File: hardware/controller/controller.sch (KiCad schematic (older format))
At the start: 54 parts, among them J1 USB_B_Micro, J2 Conn_01x12_Female, J3 Cooling fan, U1 DS3231MZ, U2 LMR16006YQ5, U3 ESP32-WROOM, U4 LMR16006YQ5, U5 CP2102N-A01-GQFN24

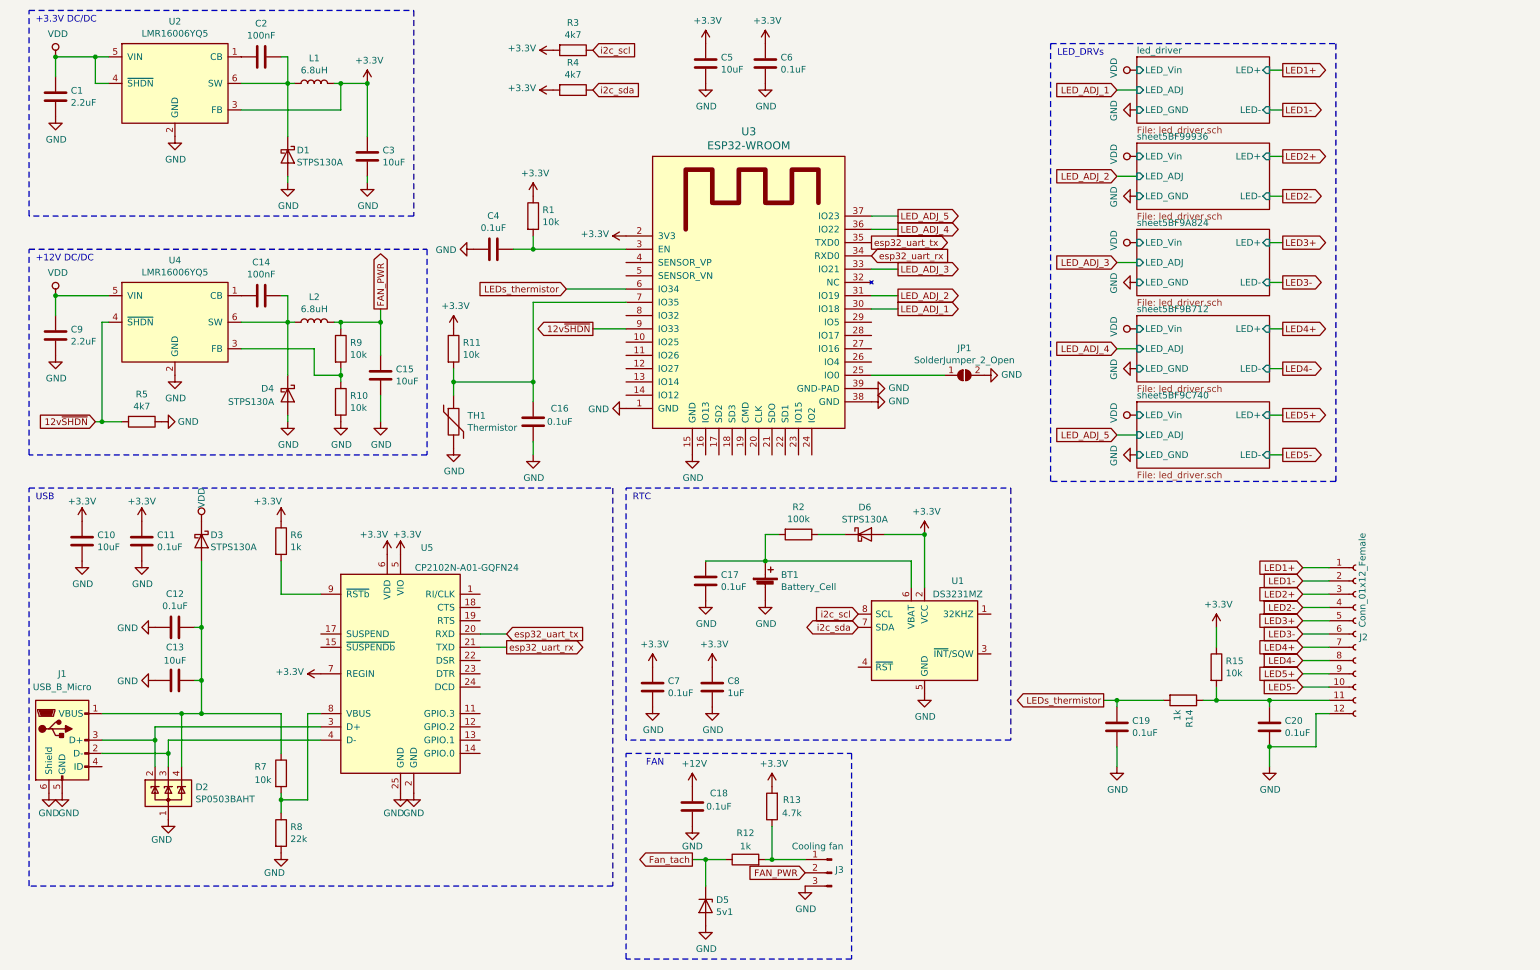
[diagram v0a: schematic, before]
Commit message: initial controller components placement
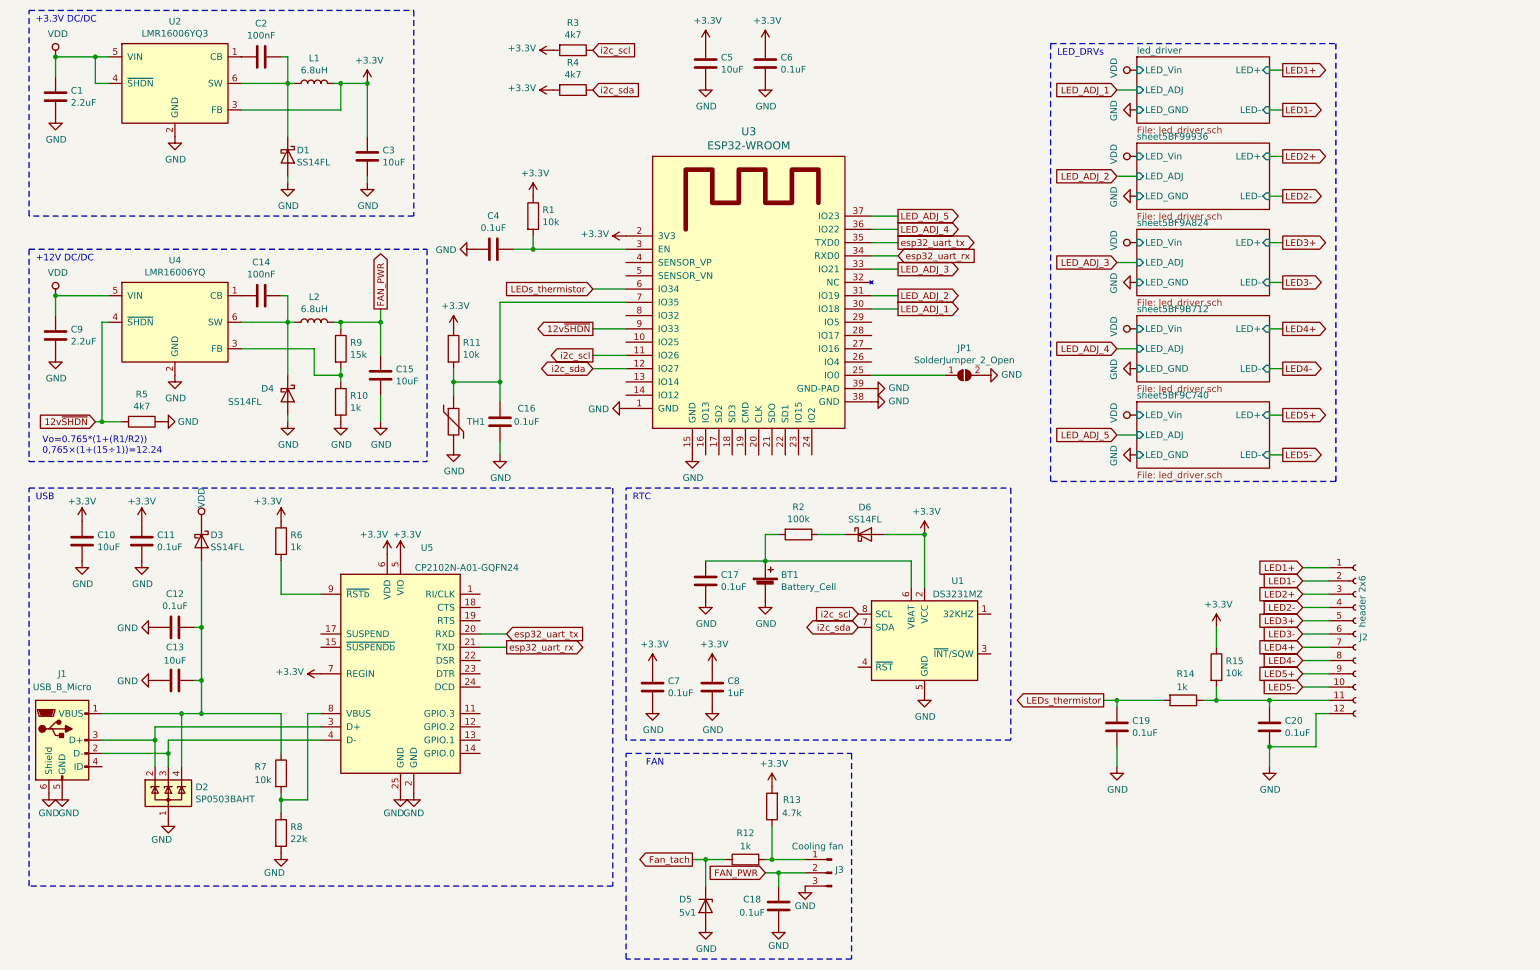
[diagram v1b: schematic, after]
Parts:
- D1, D3, D4, D6: value STPS130A -> SS14FL; footprint Diode_SMD:D_SMA -> Diode_SMD:D_SOD-123F
- J1: footprint Connector_USB:USB_Micro-B_Molex-105133-0001 -> led:USB_Micro-B_Molex-105017-0001
- J2: value Conn_01x12_Female -> header 2x6
- L1, L2: footprint Inductor_SMD:L_Wuerth_MAPI-4030 -> Inductor_SMD:L_Wuerth_MAPI-3015
- R10: value 10k -> 1k
- R9: value 10k -> 15k
- TH1: value Thermistor -> NTCS0603E3103
- U2: value LMR16006YQ5 -> LMR16006YQ3
- U4: value LMR16006YQ5 -> LMR16006YQ
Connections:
- net +12V is gone; now on net FAN_PWR: C18.2
- net i2c_scl: now also U3.11 (IO26)
- net i2c_sda: now also U3.12 (IO27)
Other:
- note added: "Vo=0.765*(1+(R1/R2))\n0,765×(1+(15÷1))=12.24"
- moved on the sheet: C16, C18
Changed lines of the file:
@@
 P 1700 1150
 F 0 "U2" H 1700 1617 50  0000 C CNN
-F 1 "LMR16006YQ5" H 1700 1526 50  0000 C CNN
+F 1 "LMR16006YQ3" H 1700 1526 50  0000 C CNN
 F 2 "Package_TO_SOT_SMD:SOT-23-6" H 1700 650 50  0001 C CIN
 F 3 "http://www.ti.com/lit/ds/symlink/lmr16006y-q1.pdf" H 1300 1600 50  0001 C CNN
@@
 F 0 "L1" V 2940 1150 50  0000 C CNN
 F 1 "6.8uH" V 2849 1150 50  0000 C CNN
-F 2 "Inductor_SMD:L_Wuerth_MAPI-4030" H 2750 1150 50  0001 C CNN
-F 3 "~" H 2750 1150 50  0001 C CNN
+F 2 "Inductor_SMD:L_Wuerth_MAPI-3015" H 2750 1150 50  0001 C CNN
+F 3 "https://katalog.we-online.de/pbs/datasheet/74438335068.pdf" H 2750 1150 50  0001 C CNN
 	1    2750 1150
 	0    -1   -1   0
@@
 P 2550 1700
 F 0 "D1" V 2504 1768 50  0000 L CNN
-F 1 "STPS130A" V 2595 1768 50  0000 L CNN
-F 2 "Diode_SMD:D_SMA" H 2550 1700 50  0001 C CNN
+F 1 "SS14FL" V 2595 1768 50  0000 L CNN
+F 2 "Diode_SMD:D_SOD-123F" H 2550 1700 50  0001 C CNN
 F 3 "~" H 2550 1700 50  0001 C CNN
 	1    2550 1700
@@
 F 0 "J1" H 850 6600 50  0000 C CNN
 F 1 "USB_B_Micro" H 850 6500 50  0000 C CNN
-F 2 "Connector_USB:USB_Micro-B_Molex-105133-0001" H 1000 6050 50  0001 C CNN
+F 2 "led:USB_Micro-B_Molex-105017-0001" H 1000 6050 50  0001 C CNN
 F 3 "~" H 1000 6050 50  0001 C CNN
 	1    850  6100
@@
 P 6900 4550
 F 0 "D6" H 6900 4755 50  0000 C CNN
-F 1 "STPS130A" H 6900 4664 50  0000 C CNN
-F 2 "Diode_SMD:D_SMA" H 6900 4550 50  0001 C CNN
+F 1 "SS14FL" H 6900 4664 50  0000 C CNN
+F 2 "Diode_SMD:D_SOD-123F" H 6900 4550 50  0001 C CNN
 F 3 "~" H 6900 4550 50  0001 C CNN
 	1    6900 4550
@@
 P 1900 4600
 F 0 "D3" V 1854 4668 50  0000 L CNN
-F 1 "STPS130A" V 1945 4668 50  0000 L CNN
-F 2 "Diode_SMD:D_SMA" H 1900 4600 50  0001 C CNN
+F 1 "SS14FL" V 1945 4668 50  0000 L CNN
+F 2 "Diode_SMD:D_SOD-123F" H 1900 4600 50  0001 C CNN
 F 3 "~" H 1900 4600 50  0001 C CNN
 	1    1900 4600
@@
 	1    0    0    -1
 $EndComp
-Text GLabel 6950 2450 2    50   Input ~ 0
+Text GLabel 7150 2450 2    50   Input ~ 0
 esp32_uart_rx
-Text GLabel 6950 2350 2    50   Output ~ 0
+Text GLabel 7150 2350 2    50   Output ~ 0
 esp32_uart_tx
 Text GLabel 4200 5400 2    50   Output ~ 0
@@
 P 10600 5300
 F 0 "J2" H 10627 5276 50  0000 L CNN
-F 1 "Conn_01x12_Female" V 10650 5350 50  0000 L CNN
+F 1 "header 2x6" V 10650 5350 50  0000 L CNN
 F 2 "Connector_PinHeader_2.54mm:PinHeader_2x06_P2.54mm_Vertical" H 10600 5300 50  0001 C CNN
 F 3 "~" H 10600 5300 50  0001 C CNN
@@
 LEDs_thermistor
 Connection ~ 9950 5800
-Text GLabel 4650 2700 0    50   Input ~ 0
+Text GLabel 4850 2700 0    50   Input ~ 0
 LEDs_thermistor
-Wire Wire Line
-	5100 2700 4650 2700
 $Comp
 L Device:R R14
 U 1 1 5BFD7FBB
 P 9300 5800
-F 0 "R14" H 9370 5846 50  0000 L CNN
-F 1 "1k" H 9370 5755 50  0000 L CNN
+F 0 "R14" V 9100 5750 50  0000 L CNN
+F 1 "1k" V 9200 5750 50  0000 L CNN
 F 2 "Resistor_SMD:R_0603_1608Metric_Pad1.05x0.95mm_HandSolder" V 9230 5800 50  0001 C CNN
 F 3 "~" H 9300 5800 50  0001 C CNN
@@
 U 1 1 5BFF6AF0
 P 3800 3700
-F 0 "TH1" H 3905 3746 50  0000 L CNN
-F 1 "Thermistor" H 3905 3655 50  0000 L CNN
+F 0 "TH1" H 3900 3700 50  0000 L CNN
+F 1 "NTCS0603E3103" H 3905 3655 50  0001 L CNN
 F 2 "Resistor_SMD:R_0603_1608Metric_Pad1.05x0.95mm_HandSolder" H 3800 3700 50  0001 C CNN
 F 3 "~" H 3800 3700 50  0001 C CNN
@@
 L Device:C C16
 U 1 1 5BFFBB68
-P 4400 3700
-F 0 "C16" H 4200 3600 50  0000 C CNN
-F 1 "0.1uF" H 4200 3700 50  0000 C CNN
-F 2 "Capacitor_SMD:C_0603_1608Metric_Pad1.05x0.95mm_HandSolder" H 4438 3550 50  0001 C CNN
-F 3 "~" H 4400 3700 50  0001 C CNN
-	1    4400 3700
+P 4150 3700
+F 0 "C16" H 3950 3600 50  0000 C CNN
+F 1 "0.1uF" H 3950 3700 50  0000 C CNN
+F 2 "Capacitor_SMD:C_0603_1608Metric_Pad1.05x0.95mm_HandSolder" H 4188 3550 50  0001 C CNN
+F 3 "~" H 4150 3700 50  0001 C CNN
+	1    4150 3700
 	-1   0    0    1
 $EndComp
@@
 L power:GND #PWR0161
 U 1 1 5BFFBC32
-P 4400 3950
-F 0 "#PWR0161" H 4400 3700 50  0001 C CNN
-F 1 "GND" H 4405 3777 50  0000 C CNN
-F 2 "" H 4400 3950 50  0001 C CNN
-F 3 "" H 4400 3950 50  0001 C CNN
-	1    4400 3950
-	1    0    0    -1
-$EndComp
-Wire Wire Line
-	5100 2800 4400 2800
-Wire Wire Line
-	4400 2800 4400 3400
+P 4150 3950
+F 0 "#PWR0161" H 4150 3700 50  0001 C CNN
+F 1 "GND" H 4155 3777 50  0000 C CNN
+F 2 "" H 4150 3950 50  0001 C CNN
+F 3 "" H 4150 3950 50  0001 C CNN
+	1    4150 3950
+	1    0    0    -1
+$EndComp
+Wire Wire Line
+	4150 2800 4150 3400
 Wire Wire Line
 	3800 3400 3800 3300
-Connection ~ 4400 3400
-Wire Wire Line
-	4400 3400 4400 3550
+Connection ~ 4150 3400
+Wire Wire Line
+	4150 3400 4150 3550
 Wire Wire Line
 	3800 3500 3800 3400
 Connection ~ 3800 3400
 Wire Wire Line
-	4400 3950 4400 3850
+	4150 3950 4150 3850
 $Comp
 L Regulator_Switching:LMR16006YQ5 U4
@@
 P 1700 2950
 F 0 "U4" H 1700 3417 50  0000 C CNN
-F 1 "LMR16006YQ5" H 1700 3326 50  0000 C CNN
+F 1 "LMR16006YQ" H 1700 3326 50  0000 C CNN
 F 2 "Package_TO_SOT_SMD:SOT-23-6" H 1700 2450 50  0001 C CIN
 F 3 "http://www.ti.com/lit/ds/symlink/lmr16006y-q1.pdf" H 1300 3400 50  0001 C CNN
@@
 F 0 "L2" V 2940 2950 50  0000 C CNN
 F 1 "6.8uH" V 2849 2950 50  0000 C CNN
-F 2 "Inductor_SMD:L_Wuerth_MAPI-4030" H 2750 2950 50  0001 C CNN
-F 3 "~" H 2750 2950 50  0001 C CNN
+F 2 "Inductor_SMD:L_Wuerth_MAPI-3015" H 2750 2950 50  0001 C CNN
+F 3 "https://katalog.we-online.de/pbs/datasheet/74438335068.pdf" H 2750 2950 50  0001 C CNN
 	1    2750 2950
 	0    -1   -1   0
@@
 P 2550 3500
 F 0 "D4" V 2500 3300 50  0000 L CNN
-F 1 "STPS130A" V 2600 3050 50  0000 L CNN
-F 2 "Diode_SMD:D_SMA" H 2550 3500 50  0001 C CNN
+F 1 "SS14FL" V 2600 3050 50  0000 L CNN
+F 2 "Diode_SMD:D_SOD-123F" H 2550 3500 50  0001 C CNN
 F 3 "~" H 2550 3500 50  0001 C CNN
 	1    2550 3500
@@
 P 2950 3150
 F 0 "R9" H 3020 3196 50  0000 L CNN
-F 1 "10k" H 3020 3105 50  0000 L CNN
+F 1 "15k" H 3020 3105 50  0000 L CNN
 F 2 "Resistor_SMD:R_0603_1608Metric_Pad1.05x0.95mm_HandSolder" V 2880 3150 50  0001 C CNN
 F 3 "~" H 2950 3150 50  0001 C CNN
@@
 $EndComp
 Wire Wire Line
-	4400 3400 3800 3400
+	4150 3400 3800 3400
 $Comp
 L Device:R R10
@@
 P 2950 3550
 F 0 "R10" H 3020 3596 50  0000 L CNN
-F 1 "10k" H 3020 3505 50  0000 L CNN
+F 1 "1k" H 3020 3505 50  0000 L CNN
 F 2 "Resistor_SMD:R_0603_1608Metric_Pad1.05x0.95mm_HandSolder" V 2880 3550 50  0001 C CNN
 F 3 "~" H 2950 3550 50  0001 C CNN
@@
 Wire Wire Line
 	3250 2950 3250 3200
-Wire Notes Line
-	600  2400 3600 2400
-Wire Notes Line
-	3600 2400 3600 3950
-Wire Notes Line
-	3600 3950 600  3950
-Wire Notes Line
-	600  3950 600  2400
 Text GLabel 1100 3700 0    50   Input ~ 0
 12v~SHDN
@@
 L Device:C C18
 U 1 1 5C071B0A
-P 5600 6600
-F 0 "C18" H 5400 6500 50  0000 C CNN
-F 1 "0.1uF" H 5400 6600 50  0000 C CNN
-F 2 "Capacitor_SMD:C_0603_1608Metric_Pad1.05x0.95mm_HandSolder" H 5638 6450 50  0001 C CNN
-F 3 "~" H 5600 6600 50  0001 C CNN
-	1    5600 6600
+P 6250 7350
+F 0 "C18" H 6450 7300 50  0000 C CNN
+F 1 "0.1uF" H 6450 7400 50  0000 C CNN
+F 2 "Capacitor_SMD:C_0603_1608Metric_Pad1.05x0.95mm_HandSolder" H 6288 7200 50  0001 C CNN
+F 3 "~" H 6250 7350 50  0001 C CNN
+	1    6250 7350
 	-1   0    0    1
 $EndComp
@@
 P 6450 7200
 F 0 "#PWR0171" H 6450 6950 50  0001 C CNN
-F 1 "GND" H 6455 7027 50  0000 C CNN
+F 1 "GND" H 6450 7050 50  0000 C CNN
 F 2 "" H 6450 7200 50  0001 C CNN
 F 3 "" H 6450 7200 50  0001 C CNN
@@
 L power:GND #PWR0172
 U 1 1 5C071FDA
-P 5600 6750
-F 0 "#PWR0172" H 5600 6500 50  0001 C CNN
-F 1 "GND" H 5600 6600 50  0000 C CNN
-F 2 "" H 5600 6750 50  0001 C CNN
-F 3 "" H 5600 6750 50  0001 C CNN
-	1    5600 6750
-	1    0    0    -1
-$EndComp
-$Comp
-L power:+12V #PWR0173
-U 1 1 5C07204B
-P 5600 6450
-F 0 "#PWR0173" H 5600 6300 50  0001 C CNN
-F 1 "+12V" H 5615 6623 50  0000 C CNN
-F 2 "" H 5600 6450 50  0001 C CNN
-F 3 "" H 5600 6450 50  0001 C CNN
-	1    5600 6450
+P 6250 7500
+F 0 "#PWR0172" H 6250 7250 50  0001 C CNN
+F 1 "GND" H 6250 7350 50  0000 C CNN
+F 2 "" H 6250 7500 50  0001 C CNN
+F 3 "" H 6250 7500 50  0001 C CNN
+	1    6250 7500
 	1    0    0    -1
 $EndComp
@@
 U 1 1 5C07F730
 P 5700 7350
-F 0 "D5" V 5654 7429 50  0000 L CNN
-F 1 "5v1" V 5745 7429 50  0000 L CNN
+F 0 "D5" V 5650 7150 50  0000 L CNN
+F 1 "5v1" V 5750 7150 50  0000 L CNN
 F 2 "Diode_SMD:D_MiniMELF" H 5700 7350 50  0001 C CNN
 F 3 "~" H 5700 7350 50  0001 C CNN
@@
 Wire Wire Line
 	6200 6750 6200 7000
-Text GLabel 6450 7100 0    50   Input ~ 0
+Text GLabel 6150 7100 0    50   Input ~ 0
 FAN_PWR
 Text GLabel 3250 2850 1    50   Output ~ 0
@@
 	3250 2950 3250 2850
 Connection ~ 3250 2950
+Wire Wire Line
+	6150 7100 6250 7100
+Wire Wire Line
+	6250 7200 6250 7100
+Connection ~ 6250 7100
+Wire Wire Line
+	6250 7100 6450 7100
+Wire Wire Line
+	4150 2800 5100 2800
+Wire Wire Line
+	6950 2350 7150 2350
+Wire Wire Line
+	6950 2450 7150 2450
+Wire Wire Line
+	4850 2700 5100 2700
+Text Notes 700  3950 0    50   ~ 0
+Vo=0.765*(1+(R1/R2))\n0,765×(1+(15÷1))=12.24
+Wire Notes Line
+	600  4000 3600 4000
+Wire Notes Line
+	3600 2400 3600 4000
+Wire Notes Line
+	600  2400 3600 2400
+Wire Notes Line
+	600  2400 600  4000
+Text GLabel 4850 3200 0    50   Output ~ 0
+i2c_scl
+Text GLabel 4850 3300 0    50   BiDi ~ 0
+i2c_sda
+Wire Wire Line
+	4850 3200 5100 3200
+Wire Wire Line
+	4850 3300 5100 3300
 $EndSCHEMATC

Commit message: open source hardware fix
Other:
- note added: "Copyright Alexander Khoroshko 2018.\nThis documentation describes Open Hardware and is licensed under the CERN OHL v. 1.2. \nYou may redistribute and modify this documentation under the terms of the CERN OHL v.1.2. \nThis documentation is distributed WITHOUT ANY EXPRESS OR IMPLIED WARRANTY, INCLUDING \nOF MERCHANTABILITY, SATISFACTORY QUALITY AND FITNESS FOR A PARTICULAR PURPOSE. \nPlease see the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"
- note added: "Reef open hardware light (ROHL) controller"
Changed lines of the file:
@@
 Wire Wire Line
 	4850 3300 5100 3300
+Text Notes 7000 7050 0    50   ~ 0
+Copyright Alexander Khoroshko 2018.\nThis   documentation   describes   Open   Hardware   and   is   licensed   under   the CERN OHL v. 1.2. \nYou may redistribute and modify this documentation under the terms of the CERN OHL v.1.2. \nThis documentation is distributed WITHOUT   ANY   EXPRESS   OR   IMPLIED   WARRANTY,   INCLUDING \nOF MERCHANTABILITY,   SATISFACTORY   QUALITY   AND   FITNESS   FOR   A PARTICULAR   PURPOSE.   \nPlease   see   the   CERN   OHL   v.1.2  for   applicable conditions.
+Text Notes 7400 7500 0    50   ~ 0
+Reef open hardware light (ROHL) controller
 $EndSCHEMATC

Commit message: controller partially traced
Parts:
- added J4: Input power, Connector:FanPinHeader_1x03_P2.54mm_Vertical, symbol Connector:Conn_01x03_Male
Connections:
- net GND: now also J4.3 (Pin_3)
- net VDD: now also J4.2 (Pin_2)
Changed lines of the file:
@@
 P 2550 3500
 F 0 "D4" V 2500 3300 50  0000 L CNN
-F 1 "SS14FL" V 2600 3050 50  0000 L CNN
+F 1 "SS14FL" V 2600 3150 50  0000 L CNN
 F 2 "Diode_SMD:D_SOD-123F" H 2550 3500 50  0001 C CNN
 F 3 "~" H 2550 3500 50  0001 C CNN
@@
 	4850 3300 5100 3300
 Text Notes 7000 7050 0    50   ~ 0
-Copyright Alexander Khoroshko 2018.\nThis   documentation   describes   Open   Hardware   and   is   licensed   under   the CERN OHL v. 1.2. \nYou may redistribute and modify this documentation under the terms of the CERN OHL v.1.2. \nThis documentation is distributed WITHOUT   ANY   EXPRESS   OR   IMPLIED   WARRANTY,   INCLUDING \nOF MERCHANTABILITY,   SATISFACTORY   QUALITY   AND   FITNESS   FOR   A PARTICULAR   PURPOSE.   \nPlease   see   the   CERN   OHL   v.1.2  for   applicable conditions.
+Copyright Alexander Khoroshko 2018.\nThis documentation describes Open Hardware and is licensed under the CERN OHL v. 1.2. \nYou may redistribute and modify this documentation under the terms of the CERN OHL v.1.2. \nThis documentation is distributed WITHOUT ANY EXPRESS OR IMPLIED WARRANTY, INCLUDING \nOF MERCHANTABILITY, SATISFACTORY QUALITY AND FITNESS FOR A PARTICULAR PURPOSE.   \nPlease see the CERN OHL v.1.2 for applicable conditions.
 Text Notes 7400 7500 0    50   ~ 0
 Reef open hardware light (ROHL) controller
+$Comp
+L Connector:Conn_01x03_Male J4
+U 1 1 5C05988F
+P 8750 4550
+F 0 "J4" H 8723 4573 50  0000 R CNN
+F 1 "Input power" H 9050 4750 50  0000 R CNN
+F 2 "Connector:FanPinHeader_1x03_P2.54mm_Vertical" H 8750 4550 50  0001 C CNN
+F 3 "~" H 8750 4550 50  0001 C CNN
+	1    8750 4550
+	-1   0    0    -1
+$EndComp
+$Comp
+L power:GND #PWR0167
+U 1 1 5C05F624
+P 8550 4650
+F 0 "#PWR0167" H 8550 4400 50  0001 C CNN
+F 1 "GND" V 8555 4477 50  0000 C CNN
+F 2 "" H 8550 4650 50  0001 C CNN
+F 3 "" H 8550 4650 50  0001 C CNN
+	1    8550 4650
+	0    1    1    0
+$EndComp
+$Comp
+L power:VDD #PWR0170
+U 1 1 5C05FBC5
+P 8550 4550
+F 0 "#PWR0170" H 8550 4400 50  0001 C CNN
+F 1 "VDD" V 8567 4723 50  0000 C CNN
+F 2 "" H 8550 4550 50  0001 C CNN
+F 3 "" H 8550 4550 50  0001 C CNN
+	1    8550 4550
+	0    -1   -1   0
+$EndComp
 $EndSCHEMATC

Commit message: controller finished. Sent both boards for manufacturing
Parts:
- D5: value 5v1 -> BZV55C5V1
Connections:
- net 12v~SHDN: now also U3.28 (IO17); no longer U3.9 (IO33)
- net usb_present: now reaches U3.24 (IO2)
- net usb_present: now also R7.2, R8.1, U5.8 (VBUS)
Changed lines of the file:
@@
 	0    -1   -1   0
 $EndComp
-Text GLabel 4850 3000 0    50   Output ~ 0
+Text GLabel 7150 3050 2    50   Output ~ 0
 12v~SHDN
 Wire Wire Line
@@
 P 5700 7350
 F 0 "D5" V 5650 7150 50  0000 L CNN
-F 1 "5v1" V 5750 7150 50  0000 L CNN
+F 1 "BZV55C5V1" V 5750 6850 50  0000 L CNN
 F 2 "Diode_SMD:D_MiniMELF" H 5700 7350 50  0001 C CNN
 F 3 "~" H 5700 7350 50  0001 C CNN
@@
 	0    -1   -1   0
 $EndComp
+Text GLabel 6450 4100 0    50   Input ~ 0
+usb_present
+Wire Wire Line
+	6500 3950 6500 4100
+Wire Wire Line
+	6500 4100 6450 4100
+Text GLabel 2800 6550 2    50   Output ~ 0
+usb_present
+Wire Wire Line
+	2700 6550 2800 6550
+Connection ~ 2700 6550
+Wire Wire Line
+	6950 3050 7150 3050
 $EndSCHEMATC
